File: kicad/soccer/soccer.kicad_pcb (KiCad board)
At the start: 2 copper layers, 350.8 x 266.6 mm, 17 parts

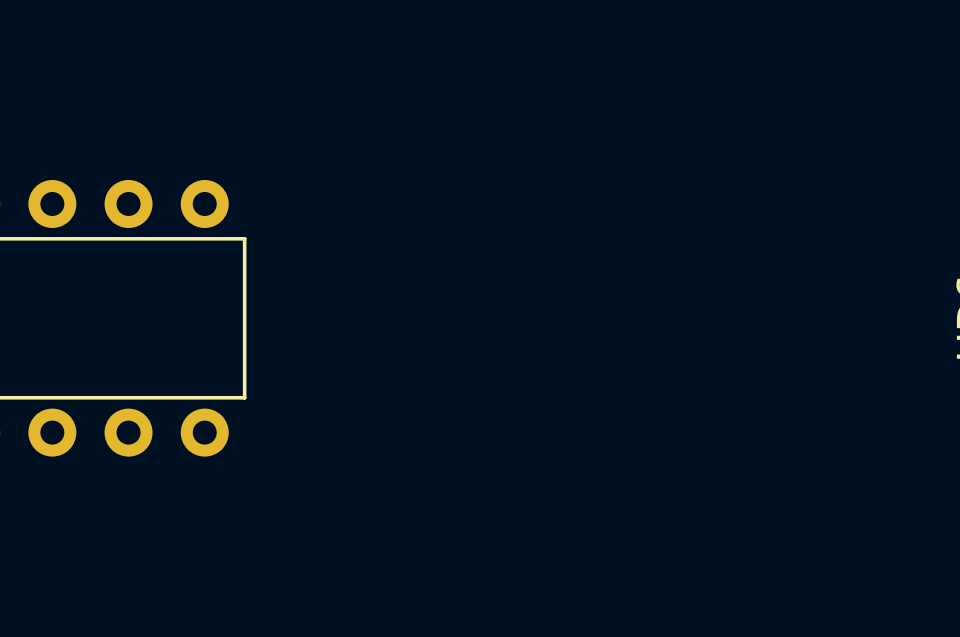
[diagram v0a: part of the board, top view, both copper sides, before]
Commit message: Teach plausible() the Fairchild parts; audit what it had decided
The last commit flagged that plausible() does not recognise the Fairchild
93xx/96xx series and left it unaudited. Audited now.

plausible() called 9312, 9316, 9321, 9322, 9300, 9301, 9334 and 9602
implausible — eight parts in 111 trusted rows and on 64 devices of published
maps, every one of them admitted by well_formed(). The two functions disagreed
about real parts, and 9316 is one this repo's own equivalence table documents
as Fairchild's 74161. Bounded to 9[36]\d{2}: a bare 9\d{3} would admit any
four-digit OCR smear.

The audit replayed the cross-printing split over every published board. 8 cells
had been decided by the filter. 4 were Asteroids P9, where a printing reading
9316 lost to one reading 74LS164 — the blind spot, discarding the more specific
reading as wreckage — and P9 is on none of the four Asteroids maps. The other 4
were the filter doing its job: 8728 to 8T28 on Football, 74LSI91 to 74LS191 on
Major Havoc, capital-I read as 1. After the fix 4 remain, all of the second
kind. No published device ever came from a false resolution.

Dropping a contested cell frees the readings a collision used to consume, so a
re-merge recovers 9 devices: Monte Carlo 3, Pole Position 4, Food Fight 1,
Soccer 1. Checked first that none of the 22 cells withdrawn last commit would
come back — every one is still reported as contested.

APB exposed a separate fault. Its 3B/F span names rows five apart, build_board
raised on it, and removing it by hand did not stick because the next merge wrote
it again — the adjacency rule lived only at build time, after the board file was
already wrong. It now runs where the designator is first accepted, and says so:
"impossible span 3B/F — those rows are not adjacent on this grid".

All 47 boards build. 2,498 devices.

Co-Authored-By: Claude Opus 5 <noreply@anthropic.com>
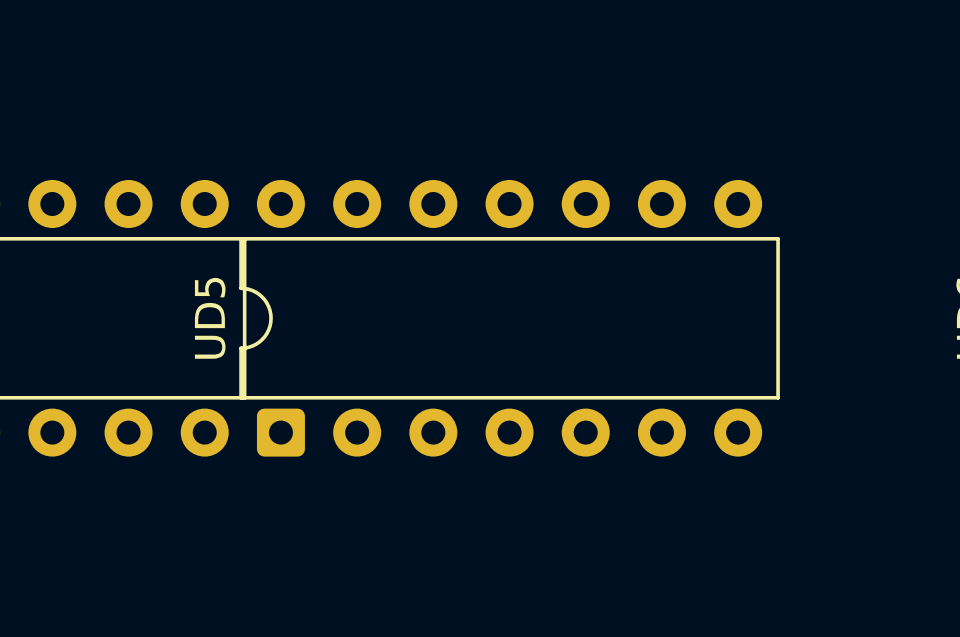
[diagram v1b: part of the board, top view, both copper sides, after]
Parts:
- added UD5: 9321, DIP-14_W7.62mm, F.Cu at (127.6, 189.4)

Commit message: Put MAME's ROM positions on the maps; let the late Asteroids boards take the lists
Two things declined earlier as decisions rather than chores, reconsidered.

The parts-list harvest never reaches memory. Atari stocks ROMs and PROMs under
its own part numbers, not as 37-series IC stock, so those rows fail the
checksum the harvest depends on — which is why Red Baron's whole complement was
missing once, and why 79 memory cells on 15 boards sat empty with everything
around them filled. MAME has them: its ROM file names encode the board
position — 035224.e2 is part 035224 at E2, 037587-01.fh1 is at the span F/H1 —
and they were checked against real boards by the people who dumped them. The
site already publishes those maps as their own asset with their own caveat.
This is that source reaching the board map under the same label, not a new one
mixed in quietly: 78 devices on 14 boards, each recorded in the chip lookup as
"MAME ROM map", only where the map had nothing. The three cells where a parts
list and MAME disagree are untouched and stay logged.

Asteroids -05 and -06 were left without the parts lists because those are
written in early designators and a direct merge would put a device one column
from where the board has it. So they take -03's parts-list additions instead,
shifted through the drawing's early-to-late table where an alternate is known
and placed at the early cell otherwise — which is exactly what these boards
already do for their 78 unshifted drawing-read devices, under a caveat they
already carry. 13 each. None of the 22 turned out to have a known alternate,
and 9 land on cells a shifted device already occupies and are skipped rather
than duplicated. All of it runs inside the generator, so it survives
regeneration.

50 boards, 2,672 devices.

Co-Authored-By: Claude Fable 5.1 <noreply@anthropic.com>
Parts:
- added UE2: 035224, DIP-14_W7.62mm, F.Cu at (51.4, 170.4)
- added UF2: 035225, DIP-14_W7.62mm, F.Cu at (51.4, 151.3)
- added UH2: 035228, DIP-14_W7.62mm, F.Cu at (51.4, 132.3)
- added UJ2: 035229, DIP-14_W7.62mm, F.Cu at (51.4, 113.2)
- added UK2: 035232, DIP-14_W7.62mm, F.Cu at (51.4, 94.2)
- added UL2: 035233, DIP-14_W7.62mm, F.Cu at (51.4, 75.2)
- added UM2: 035236, DIP-14_W7.62mm, F.Cu at (51.4, 56.1)
- added UM7: 035248, DIP-14_W7.62mm, F.Cu at (178.4, 56.1)
- added UN2: 035237, DIP-14_W7.62mm, F.Cu at (51.4, 37.0)
- added UN4: 34006-01, DIP-14_W7.62mm, F.Cu at (102.2, 37.0)
